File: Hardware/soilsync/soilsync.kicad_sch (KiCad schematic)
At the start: 48 parts, among them J1 Barrel_Jack_Switch, J10 Screw_Terminal_01x03, J11 Screw_Terminal_01x03, J12 Screw_Terminal_01x03, J13 Conn_Battery, J14 BMS_Terminal, J15 Conn_01x04_Socket, J2 Screw_Terminal_01x03, J3 Screw_Terminal_01x03, J4 Screw_Terminal_01x03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

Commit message: PCB Finished
Generated fabrication data
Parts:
- removed C1: 100n, Capacitor_SMD:C_1206_3216Metric_Pad1.33x1.80mm_HandSolder, symbol Device:C
- removed D1, D2: MBR340, Diode_THT:D_DO-201AD_P15.24mm_Horizontal, symbol Diode:MBR340
- removed J12: Screw_Terminal_01x03, TerminalBlock_4Ucon:TerminalBlock_4Ucon_1x03_P3.50mm_Horizontal, symbol Connector:Screw_Terminal_01x03
- removed J15: Conn_01x04_Socket, Connector_PinSocket_2.54mm:PinSocket_1x04_P2.54mm_Vertical, symbol Connector:Conn_01x04_Socket
- removed R21: 10k, Resistor_SMD:R_1206_3216Metric_Pad1.30x1.75mm_HandSolder, symbol Device:R
- removed U1: STM32F103C8Tx, Package_QFP:LQFP-48_7x7mm_P0.5mm, symbol MCU_ST_STM32F1:STM32F103C8Tx
- added D1, D2, D4: MBRS340, Diode_SMD:D_SMC, symbol Diode:MBRS340
- added J12: PUMP_Terminal, TerminalBlock_4Ucon:TerminalBlock_4Ucon_1x02_P3.50mm_Horizontal, symbol Connector:Screw_Terminal_01x02
- added U1: YAAJ_BluePill, STM32_Footprints:YAAJ_BluePill_1, symbol YAAJ_BluePill:YAAJ_BluePill
- R22: footprint (none) -> Resistor_SMD:R_1206_3216Metric_Pad1.30x1.75mm_HandSolder
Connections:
- net +3.3V: now also U1.20 (3V3), U1.38 (3V3)
- net +5V: now also D4.1 (K), J12.1 (Pin_1)
- net BAT+: now also D2.2 (A)
- net GND: now also U1.19 (GND), U1.39 (GND), U1.40 (GND)
- net NRF_CE: now also U1.5 (PA8)
- net NRF_CSN: now also U1.1 (PB12)
- net NRF_MISO: now also U1.3 (PB14)
- net NRF_MOSI: now also U1.4 (PB15)
- net NRF_SCK: now also U1.2 (PB13)
- net PUMP: now also U1.12 (PB4)
- net SENSOR_1: now also U1.25 (PA0)
- net SENSOR_10: now also U1.34 (PB1)
- net SENSOR_2: now also U1.26 (PA1)
- net SENSOR_3: now also U1.27 (PA2)
- net SENSOR_4: now also U1.28 (PA3)
- net SENSOR_5: now also U1.29 (PA4)
- net SENSOR_6: now also U1.30 (PA5)
- net SENSOR_7: now also U1.31 (PA6)
- net SENSOR_8: now also U1.32 (PA7)
- net SENSOR_9: now also U1.33 (PB0)
- net VIN: now also D1.1 (K), D2.1 (K)
- net at J1.1: now also D1.2 (A)
- net at J13.1 (Pin_1): no longer U6.2 (B-)
- net at J13.2 (Pin_2): no longer U6.5 (BM)
- net PUMP-: now reaches Q1.2 (D)
- net PUMP-: now also D4.2 (A), J12.2 (Pin_2)
- no-connect marks 20 -> 22
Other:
- moved on the sheet: J14, Q1, R22, U4

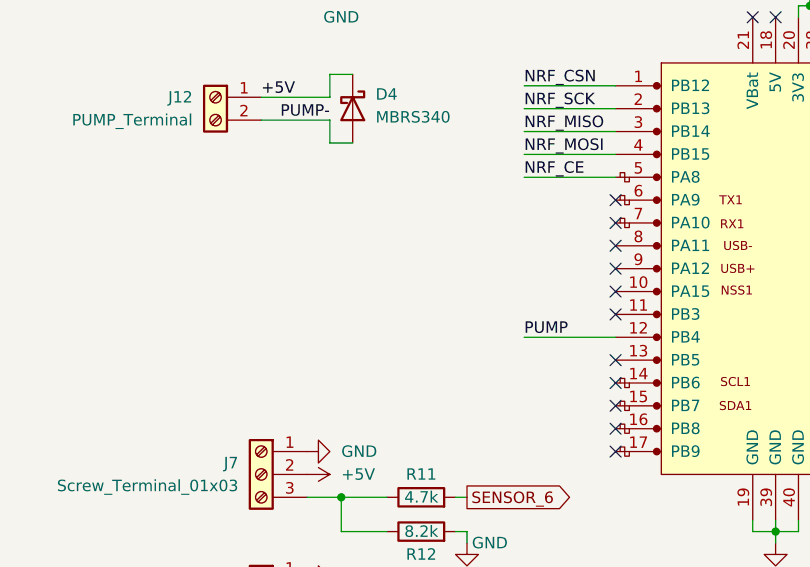
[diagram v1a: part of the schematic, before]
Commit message: added Servo pin headers
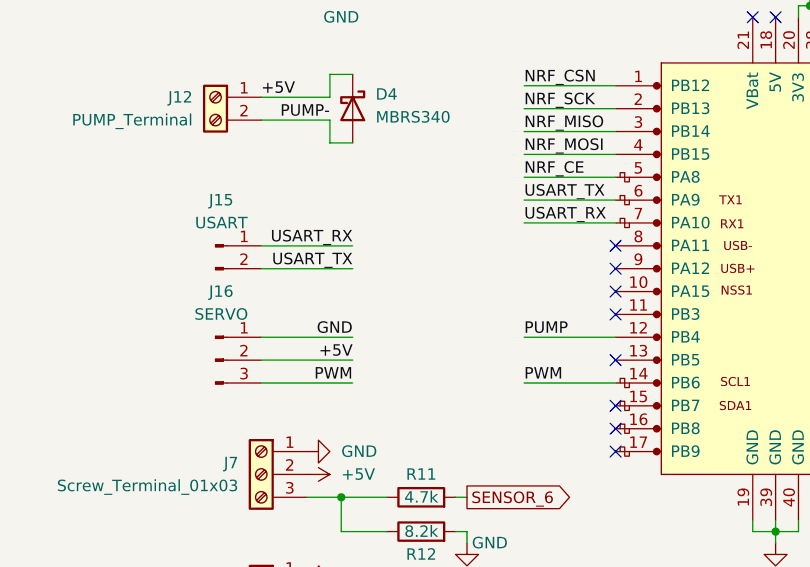
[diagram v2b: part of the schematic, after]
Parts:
- added J15: USART, Connector_PinHeader_2.54mm:PinHeader_1x02_P2.54mm_Vertical, symbol Connector:Conn_01x02_Pin
- added J16: SERVO, Connector_PinHeader_2.54mm:PinHeader_1x03_P2.54mm_Vertical, symbol Connector:Conn_01x03_Pin
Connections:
- net +5V: now also J16.2 (Pin_2)
- net GND: now also J16.1 (Pin_1)
- net PWM: now reaches U1.14 (PB6)
- net PWM: now also J16.3 (Pin_3)
- net USART_TX: now reaches U1.6 (PA9)
- net USART_TX: now also J15.2 (Pin_2)
- net USART_RX: now reaches U1.7 (PA10)
- net USART_RX: now also J15.1 (Pin_1)
- no-connect marks 22 -> 19
